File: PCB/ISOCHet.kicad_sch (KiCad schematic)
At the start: 19 parts, among them J1 USB_C_Receptacle_USB2.0, J2 Conn_01x08_Pin, SW0 BOOT, SW1 TAB, SW2 ENTER, SW3 CAPS, SW4 CAPS_STEP1.5, SW5 CAPS_STEP1.25, U1 CH552G, U2 USBLC6-2P6

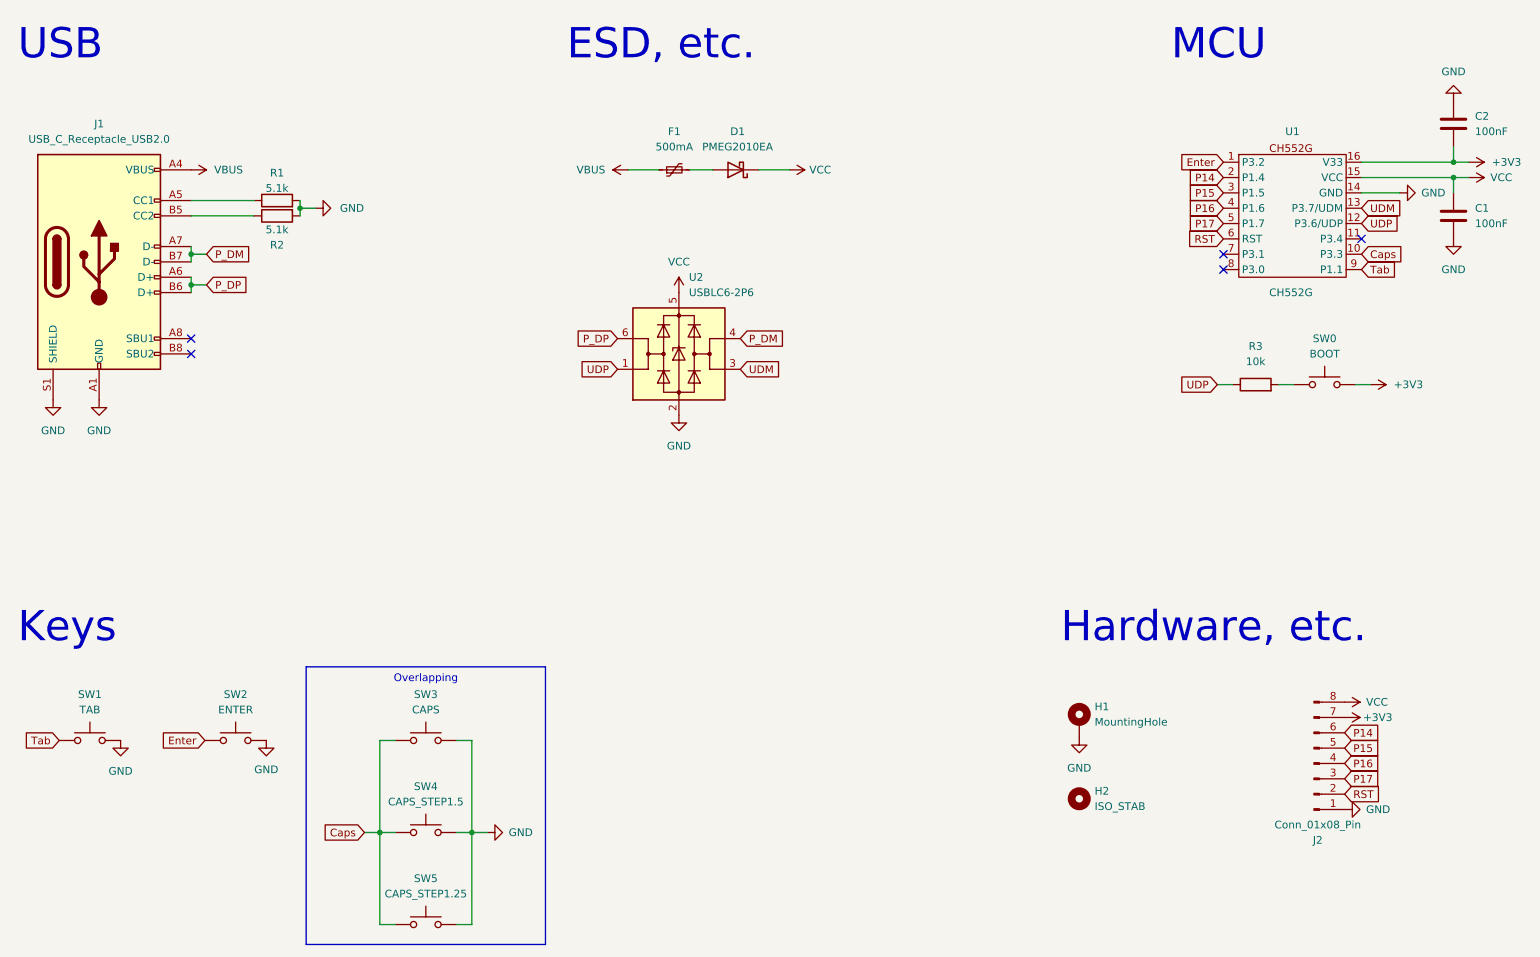
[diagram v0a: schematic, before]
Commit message: Rotated CH552 90° and rerouted accordingly
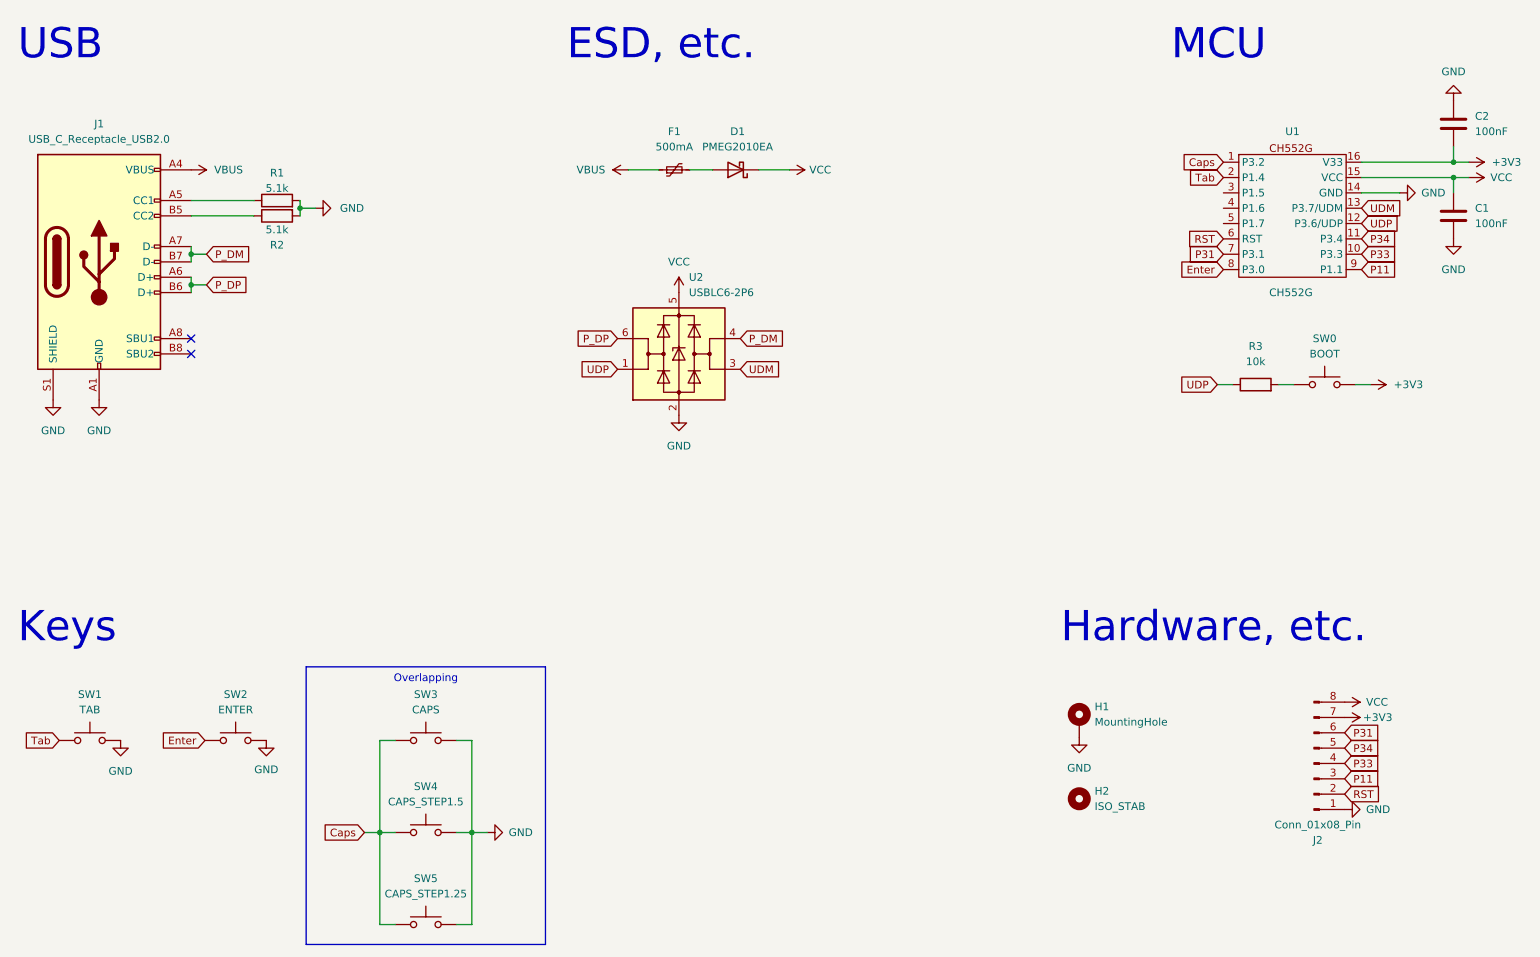
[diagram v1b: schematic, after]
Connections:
- net Caps: now also SW3.2, SW4.2, SW5.2, U1.1 (P3.2); no longer SW3.1, SW4.1, SW5.1, U1.10 (P3.3)
- net Enter: now also U1.8 (P3.0); no longer U1.1 (P3.2)
- net GND: now also SW1.1, SW3.1, SW4.1, SW5.1; no longer SW1.2, SW3.2, SW4.2, SW5.2
- net Tab: now also SW1.2, U1.2 (P1.4); no longer SW1.1, U1.9 (P1.1)
- net P34: now reaches U1.11 (P3.4)
- net P34: now also J2.5 (Pin_5)
- net P31: now reaches U1.7 (P3.1)
- net P31: now also J2.6 (Pin_6)
- removed net P14: J2.6 (Pin_6), U1.2 (P1.4)
- net P15: no longer names the net of U1.3 (P1.5)
- net P15: no longer J2.5 (Pin_5)
- net P16: no longer names the net of U1.4 (P1.6)
- net P16: no longer J2.4 (Pin_4)
- net P17: no longer names the net of U1.5 (P1.7)
- net P17: no longer J2.3 (Pin_3)
- new net P11: J2.3 (Pin_3), U1.9 (P1.1)
- new net P33: J2.4 (Pin_4), U1.10 (P3.3)
- no-connect marks 5 -> 2
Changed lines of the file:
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@@
   (junction (at 77.724 150.368) (diameter 0) (color 0 0 0 0)
   )
-  (no_connect (at 217.424 57.15))
-  (no_connect (at 217.424 54.61))
   (no_connect (at 46.482 71.12))
-  (no_connect (at 240.284 52.07))
   (no_connect (at 46.482 68.58))
   (wire (pts (xy 140.462 40.64) (xy 145.542 40.64))
@@
     )
   )
+  (global_label "Caps" (shape input) (at 217.424 39.37 180) (fields_autoplaced)
+    (effects (font (size 1.27 1.27)) (justify right))
+    (property "Intersheetrefs" "${INTERSHEET_REFS}" (at 209.8427 39.37 0)
+      (effects (font (size 1.27 1.27)) (justify right) hide)
+    )
+  )
   (global_label "UDP" (shape input) (at 240.284 49.53 0) (fields_autoplaced)
     (effects (font (size 1.27 1.27)) (justify left))
@@
     )
   )
-  (global_label "Tab" (shape input) (at 240.284 57.15 0) (fields_autoplaced)
-    (effects (font (size 1.27 1.27)) (justify left))
-    (property "Intersheetrefs" "${INTERSHEET_REFS}" (at 246.5348 57.15 0)
-      (effects (font (size 1.27 1.27)) (justify left) hide)
+  (global_label "Tab" (shape input) (at 217.424 41.91 180) (fields_autoplaced)
+    (effects (font (size 1.27 1.27)) (justify right))
+    (property "Intersheetrefs" "${INTERSHEET_REFS}" (at 211.1732 41.91 0)
+      (effects (font (size 1.27 1.27)) (justify right) hide)
     )
   )
@@
     )
   )
-  (global_label "P16" (shape input) (at 217.424 46.99 180) (fields_autoplaced)
-    (effects (font (size 1.27 1.27)) (justify right))
-    (property "Intersheetrefs" "${INTERSHEET_REFS}" (at 210.7498 46.99 0)
-      (effects (font (size 1.27 1.27)) (justify right) hide)
+  (global_label "P33" (shape input) (at 240.284 54.61 0) (fields_autoplaced)
+    (effects (font (size 1.27 1.27)) (justify left))
+    (property "Intersheetrefs" "${INTERSHEET_REFS}" (at 246.9582 54.61 0)
+      (effects (font (size 1.27 1.27)) (justify left) hide)
     )
   )
@@
     )
   )
-  (global_label "Caps" (shape input) (at 240.284 54.61 0) (fields_autoplaced)
-    (effects (font (size 1.27 1.27)) (justify left))
-    (property "Intersheetrefs" "${INTERSHEET_REFS}" (at 247.8653 54.61 0)
-      (effects (font (size 1.27 1.27)) (justify left) hide)
-    )
-  )
   (global_label "RST" (shape input) (at 237.49 144.018 0) (fields_autoplaced)
     (effects (font (size 1.27 1.27)) (justify left))
@@
     )
   )
-  (global_label "P17" (shape input) (at 217.424 49.53 180) (fields_autoplaced)
-    (effects (font (size 1.27 1.27)) (justify right))
-    (property "Intersheetrefs" "${INTERSHEET_REFS}" (at 210.7498 49.53 0)
-      (effects (font (size 1.27 1.27)) (justify right) hide)
-    )
-  )
-  (global_label "P16" (shape input) (at 237.49 138.938 0) (fields_autoplaced)
+  (global_label "P11" (shape input) (at 240.284 57.15 0) (fields_autoplaced)
+    (effects (font (size 1.27 1.27)) (justify left))
+    (property "Intersheetrefs" "${INTERSHEET_REFS}" (at 246.9582 57.15 0)
+      (effects (font (size 1.27 1.27)) (justify left) hide)
+    )
+  )
+  (global_label "Enter" (shape input) (at 217.424 57.15 180) (fields_autoplaced)
+    (effects (font (size 1.27 1.27)) (justify right))
+    (property "Intersheetrefs" "${INTERSHEET_REFS}" (at 209.5403 57.15 0)
+      (effects (font (size 1.27 1.27)) (justify right) hide)
+    )
+  )
+  (global_label "P33" (shape input) (at 237.49 138.938 0) (fields_autoplaced)
     (effects (font (size 1.27 1.27)) (justify left))
     (property "Intersheetrefs" "${INTERSHEET_REFS}" (at 244.1642 138.938 0)
@@
     )
   )
-  (global_label "P15" (shape input) (at 217.424 44.45 180) (fields_autoplaced)
-    (effects (font (size 1.27 1.27)) (justify right))
-    (property "Intersheetrefs" "${INTERSHEET_REFS}" (at 210.7498 44.45 0)
-      (effects (font (size 1.27 1.27)) (justify right) hide)
-    )
-  )
-  (global_label "P15" (shape input) (at 237.49 136.398 0) (fields_autoplaced)
+  (global_label "P34" (shape input) (at 240.284 52.07 0) (fields_autoplaced)
+    (effects (font (size 1.27 1.27)) (justify left))
+    (property "Intersheetrefs" "${INTERSHEET_REFS}" (at 246.9582 52.07 0)
+      (effects (font (size 1.27 1.27)) (justify left) hide)
+    )
+  )
+  (global_label "P34" (shape input) (at 237.49 136.398 0) (fields_autoplaced)
     (effects (font (size 1.27 1.27)) (justify left))
     (property "Intersheetrefs" "${INTERSHEET_REFS}" (at 244.1642 136.398 0)
@@
     )
   )
-  (global_label "P14" (shape input) (at 217.424 41.91 180) (fields_autoplaced)
-    (effects (font (size 1.27 1.27)) (justify right))
-    (property "Intersheetrefs" "${INTERSHEET_REFS}" (at 210.7498 41.91 0)
-      (effects (font (size 1.27 1.27)) (justify right) hide)
-    )
-  )
-  (global_label "P17" (shape input) (at 237.49 141.478 0) (fields_autoplaced)
+  (global_label "P31" (shape input) (at 217.424 54.61 180) (fields_autoplaced)
+    (effects (font (size 1.27 1.27)) (justify right))
+    (property "Intersheetrefs" "${INTERSHEET_REFS}" (at 210.7498 54.61 0)
+      (effects (font (size 1.27 1.27)) (justify right) hide)
+    )
+  )
+  (global_label "P11" (shape input) (at 237.49 141.478 0) (fields_autoplaced)
     (effects (font (size 1.27 1.27)) (justify left))
     (property "Intersheetrefs" "${INTERSHEET_REFS}" (at 244.1642 141.478 0)
@@
     )
   )
-  (global_label "P14" (shape input) (at 237.49 133.858 0) (fields_autoplaced)
+  (global_label "P31" (shape input) (at 237.49 133.858 0) (fields_autoplaced)
     (effects (font (size 1.27 1.27)) (justify left))
     (property "Intersheetrefs" "${INTERSHEET_REFS}" (at 244.1642 133.858 0)
@@
     (effects (font (size 1.27 1.27)) (justify right))
     (property "Intersheetrefs" "${INTERSHEET_REFS}" (at 40.8843 135.128 0)
-      (effects (font (size 1.27 1.27)) (justify right) hide)
-    )
-  )
-  (global_label "Enter" (shape input) (at 217.424 39.37 180) (fields_autoplaced)
-    (effects (font (size 1.27 1.27)) (justify right))
-    (property "Intersheetrefs" "${INTERSHEET_REFS}" (at 209.5403 39.37 0)
       (effects (font (size 1.27 1.27)) (justify right) hide)
     )
@@
     )
   )
-  (symbol (lib_id "Switch:SW_Push") (at 85.344 165.608 0) (unit 1)
-    (in_bom no) (on_board yes) (dnp no) (fields_autoplaced)
+  (symbol (lib_id "Switch:SW_Push") (at 85.344 165.608 0) (mirror y) (unit 1)
+    (in_bom no) (on_board yes) (dnp no)
     (property "Reference" "SW5" (at 85.344 157.988 0)
       (effects (font (size 1.27 1.27)))
@@
     )
   )
-  (symbol (lib_id "Switch:SW_Push") (at 85.344 150.368 0) (unit 1)
-    (in_bom no) (on_board yes) (dnp no) (fields_autoplaced)
+  (symbol (lib_id "Switch:SW_Push") (at 85.344 150.368 0) (mirror y) (unit 1)
+    (in_bom no) (on_board yes) (dnp no)
     (property "Reference" "SW4" (at 85.344 142.748 0)
       (effects (font (size 1.27 1.27)))
@@
     )
   )
-  (symbol (lib_id "Switch:SW_Push") (at 85.344 135.128 0) (unit 1)
-    (in_bom yes) (on_board yes) (dnp no) (fields_autoplaced)
+  (symbol (lib_id "Switch:SW_Push") (at 85.344 135.128 0) (mirror y) (unit 1)
+    (in_bom yes) (on_board yes) (dnp no)
     (property "Reference" "SW3" (at 85.344 127.508 0)
       (effects (font (size 1.27 1.27)))
@@
     )
   )
-  (symbol (lib_id "Switch:SW_Push") (at 29.718 135.128 0) (unit 1)
-    (in_bom yes) (on_board yes) (dnp no) (fields_autoplaced)
+  (symbol (lib_id "Switch:SW_Push") (at 29.718 135.128 0) (mirror y) (unit 1)
+    (in_bom yes) (on_board yes) (dnp no)
     (property "Reference" "SW1" (at 29.718 127.508 0)
       (effects (font (size 1.27 1.27)))

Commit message: Create draft of version using CH552E
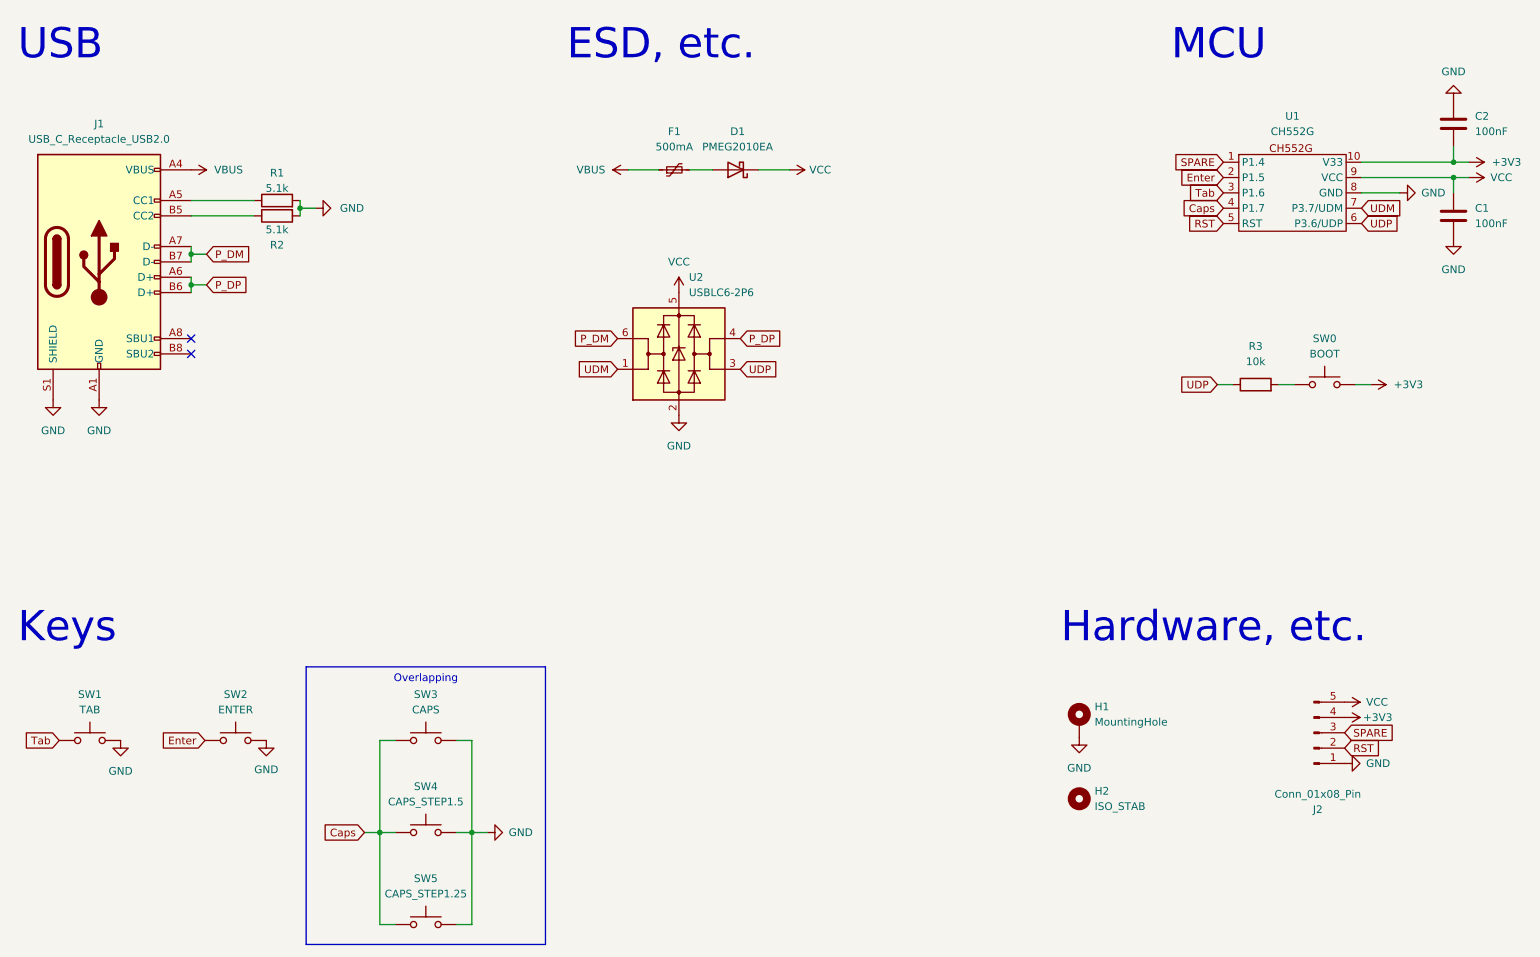
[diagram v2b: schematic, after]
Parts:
- J2: footprint Connector_PinHeader_2.00mm:PinHeader_1x08_P2.00mm_Vertical -> Connector_PinHeader_2.00mm:PinHeader_1x05_P2.00mm_Vertical; symbol Connector:Conn_01x08_Pin -> Connector:Conn_01x05_Pin; now in the parts list
- U1: footprint Package_SO:SOP-16_3.9x9.9mm_P1.27mm -> Package_SO:MSOP-10_3x3mm_P0.5mm; symbol Project Library:MCU_CM552G_SOP-16 -> Project Library:MCU_CM552E_MSOP-10
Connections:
- net P33 is gone; now on net +3V3: J2.4 (Pin_4), U1.10 (V33)
- net +3V3: no longer J2.7 (Pin_7), U1.16 (V33)
- net Caps: now also U1.4 (P1.7); no longer U1.1 (P3.2)
- net Enter: now also U1.2 (P1.5); no longer U1.8 (P3.0)
- net GND: now also U1.8 (GND); no longer U1.14 (GND)
- net P_DM: now also U2.6 (I/O1); no longer U2.4 (I/O2)
- net P_DP: now also U2.4 (I/O2); no longer U2.6 (I/O1)
- net RST: now also U1.5 (RST); no longer U1.6 (RST)
- net Tab: now also U1.3 (P1.6); no longer U1.2 (P1.4)
- net UDM: now also U1.7 (P3.7/UDM), U2.1 (I/O1); no longer U1.13 (P3.7/UDM), U2.3 (I/O2)
- net UDP: now also U1.6 (P3.6/UDP), U2.3 (I/O2); no longer U1.12 (P3.6/UDP), U2.1 (I/O1)
- net VCC: now also J2.5 (Pin_5), U1.9 (VCC); no longer J2.8 (Pin_8), U1.15 (VCC)
- net P11 renamed SPARE
- net SPARE: now also U1.1 (P1.4); no longer U1.9 (P1.1)
- removed net P31: J2.6 (Pin_6), U1.7 (P3.1)
- removed net P34: J2.5 (Pin_5), U1.11 (P3.4)
